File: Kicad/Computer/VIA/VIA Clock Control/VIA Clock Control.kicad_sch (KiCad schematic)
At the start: 14 parts, among them IC10 74LVC1G157GV-Q100H, IC2 AP7365-33WG-7, IC7 74LVC74APW,118, IC8 74LVC257APW,118, IC9 74LVC257APW,118, J1 Conn_02x16_Counter_Clockwise

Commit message: Added a VIA Board.
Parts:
- J1: footprint SamacSys_Parts:DIP-32_Board_W22.86mm -> SamacSys_Parts:DIP-32_Board_W15.24mm
- renumbered R1 to R2
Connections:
- net 5V: now also J1.1 (Pin_1), J1.17 (Pin_17); no longer J1.24 (Pin_24), J1.8 (Pin_8)
- net CH0_{OUT}: now also J1.29 (Pin_29); no longer J1.28 (Pin_28)
- net CH1_{OUT}: now also J1.30 (Pin_30); no longer J1.29 (Pin_29)
- net CH2_{OUT}: now also J1.31 (Pin_31); no longer J1.30 (Pin_30)
- net GND: now also J1.13 (Pin_13), J1.20 (Pin_20), J1.28 (Pin_28), J1.5 (Pin_5); no longer J1.15 (Pin_15), J1.18 (Pin_18), J1.2 (Pin_2), J1.31 (Pin_31)
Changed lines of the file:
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@@
   (junction (at 196.85 59.055) (diameter 0) (color 0 0 0 0)
   )
-  (no_connect (at 4.445 48.26))
+  (no_connect (at 4.445 50.8))
   (no_connect (at 4.445 76.2))
-  (no_connect (at 4.445 78.74))
+  (no_connect (at 4.445 83.82))
   (no_connect (at 4.445 86.36))
   (no_connect (at 17.145 48.26))
   (no_connect (at 17.145 73.66))
   (no_connect (at 4.445 71.12))
-  (no_connect (at 17.145 78.74))
+  (no_connect (at 17.145 68.58))
   (no_connect (at 17.145 63.5))
   (no_connect (at 17.145 81.28))
-  (no_connect (at 17.145 86.36))
+  (no_connect (at 17.145 83.82))
   (no_connect (at 17.145 60.96))
   (no_connect (at 4.445 81.28))
@@
   (no_connect (at 128.27 139.7))
   (no_connect (at 94.615 63.5))
-  (no_connect (at 4.445 58.42))
+  (no_connect (at 4.445 66.04))
   (no_connect (at 4.445 73.66))
   (no_connect (at 222.25 64.135))
@@
     (effects (font (size 1.27 1.27)) (justify right bottom))
   )
-  (label "CH0_{OUT}" (at 17.145 58.42 0) (fields_autoplaced)
+  (label "CH0_{OUT}" (at 17.145 55.88 0) (fields_autoplaced)
     (effects (font (size 1.27 1.27)) (justify left bottom))
   )
@@
     (effects (font (size 1.27 1.27)) (justify left bottom))
   )
+  (label "GND" (at 4.445 78.74 180) (fields_autoplaced)
+    (effects (font (size 1.27 1.27)) (justify right bottom))
+  )
   (label "CLK÷2" (at 56.515 96.52 180) (fields_autoplaced)
     (effects (font (size 1.27 1.27)) (justify right bottom))
@@
     (effects (font (size 1.27 1.27)) (justify right bottom))
   )
-  (label "CH1_{OUT}" (at 17.145 55.88 0) (fields_autoplaced)
-    (effects (font (size 1.27 1.27)) (justify left bottom))
+  (label "CH1_{OUT}" (at 17.145 53.34 0) (fields_autoplaced)
+    (effects (font (size 1.27 1.27)) (justify left bottom))
+  )
+  (label "GND" (at 4.445 58.42 180) (fields_autoplaced)
+    (effects (font (size 1.27 1.27)) (justify right bottom))
   )
   (label "GND" (at 56.515 121.92 180) (fields_autoplaced)
@@
     (effects (font (size 1.27 1.27)) (justify right bottom))
   )
+  (label "GND" (at 17.145 58.42 0) (fields_autoplaced)
+    (effects (font (size 1.27 1.27)) (justify left bottom))
+  )
   (label "GND" (at 104.775 71.755 0) (fields_autoplaced)
     (effects (font (size 1.27 1.27)) (justify left bottom))
@@
     (effects (font (size 1.27 1.27)) (justify right bottom))
   )
-  (label "GND" (at 4.445 83.82 180) (fields_autoplaced)
-    (effects (font (size 1.27 1.27)) (justify right bottom))
+  (label "GND" (at 17.145 78.74 0) (fields_autoplaced)
+    (effects (font (size 1.27 1.27)) (justify left bottom))
   )
   (label "GND" (at 69.215 60.96 180) (fields_autoplaced)
@@
     (effects (font (size 1.27 1.27)) (justify right bottom))
   )
-  (label "5V" (at 4.445 66.04 180) (fields_autoplaced)
+  (label "5V" (at 4.445 48.26 180) (fields_autoplaced)
     (effects (font (size 1.27 1.27)) (justify right bottom))
   )
@@
     (effects (font (size 1.27 1.27)) (justify left bottom))
   )
-  (label "GND" (at 17.145 83.82 0) (fields_autoplaced)
-    (effects (font (size 1.27 1.27)) (justify left bottom))
-  )
-  (label "5V" (at 17.145 68.58 0) (fields_autoplaced)
-    (effects (font (size 1.27 1.27)) (justify left bottom))
-  )
   (label "Select CLK÷2" (at 29.21 124.46 0) (fields_autoplaced)
     (effects (font (size 1.27 1.27)) (justify left bottom))
@@
     (effects (font (size 1.27 1.27)) (justify left bottom))
   )
-  (label "GND" (at 17.145 50.8 0) (fields_autoplaced)
+  (label "5V" (at 17.145 86.36 0) (fields_autoplaced)
     (effects (font (size 1.27 1.27)) (justify left bottom))
   )
@@
     (effects (font (size 1.27 1.27)) (justify right bottom))
   )
-  (label "CH2_{OUT}" (at 17.145 53.34 0) (fields_autoplaced)
+  (label "CH2_{OUT}" (at 17.145 50.8 0) (fields_autoplaced)
     (effects (font (size 1.27 1.27)) (justify left bottom))
   )
@@
     (effects (font (size 1.27 1.27)) (justify right bottom))
   )
-  (label "GND" (at 4.445 50.8 180) (fields_autoplaced)
-    (effects (font (size 1.27 1.27)) (justify right bottom))
-  )
   (label "~{Reset}" (at 69.215 68.58 180) (fields_autoplaced)
     (effects (font (size 1.27 1.27)) (justify right bottom))
@@
   (symbol (lib_id "HCP65:R_0805") (at 26.035 118.11 270) (unit 1)
     (in_bom yes) (on_board yes) (dnp no)
-    (property "Reference" "R1" (at 27.813 120.65 0)
+    (property "Reference" "R2" (at 27.813 120.65 0)
       (effects (font (size 1.27 1.27)))
     )
@@
     (pin "2")
     (instances
-      (project "Via Clock Control"
+      (project "VIA Clock Control"
         (path "/582a2c40-9bf2-463e-b0f7-d7ac5e4fbba5"
           (reference "R2") (unit 1)
@@
         )
       )
-      (project "Via Clock Control"
+      (project "VIA Clock Control"
         (path "/582a2c40-9bf2-463e-b0f7-d7ac5e4fbba5"
           (reference "C1") (unit 1)
@@
         )
       )
-      (project "Via Clock Control"
+      (project "VIA Clock Control"
         (path "/582a2c40-9bf2-463e-b0f7-d7ac5e4fbba5"
           (reference "IC5") (unit 1)
@@
         )
       )
-      (project "Via Clock Control"
+      (project "VIA Clock Control"
         (path "/582a2c40-9bf2-463e-b0f7-d7ac5e4fbba5"
           (reference "C2") (unit 1)
@@
     (pin "N2")
     (instances
-      (project "Via Clock Control"
+      (project "VIA Clock Control"
         (path "/582a2c40-9bf2-463e-b0f7-d7ac5e4fbba5"
           (reference "S1") (unit 1)
@@
         )
       )
-      (project "Via Clock Control"
+      (project "VIA Clock Control"
         (path "/582a2c40-9bf2-463e-b0f7-d7ac5e4fbba5"
           (reference "C4") (unit 1)
@@
         )
       )
-      (project "Via Clock Control"
+      (project "VIA Clock Control"
         (path "/582a2c40-9bf2-463e-b0f7-d7ac5e4fbba5"
           (reference "C6") (unit 1)
@@
     (pin "15")
     (instances
-      (project "Via Clock Control"
+      (project "VIA Clock Control"
         (path "/582a2c40-9bf2-463e-b0f7-d7ac5e4fbba5"
           (reference "IC8") (unit 1)
@@
       (effects (font (size 1.27 1.27)))
     )
-    (property "Footprint" "SamacSys_Parts:DIP-32_Board_W22.86mm" (at 9.525 66.04 0)
+    (property "Footprint" "SamacSys_Parts:DIP-32_Board_W15.24mm" (at 9.525 66.04 0)
       (effects (font (size 1.27 1.27)) hide)
     )
@@
         )
       )
-      (project "Via Clock Control"
+      (project "VIA Clock Control"
         (path "/582a2c40-9bf2-463e-b0f7-d7ac5e4fbba5"
           (reference "J3") (unit 1)
@@
     (pin "15")
     (instances
-      (project "Via Clock Control"
+      (project "VIA Clock Control"
         (path "/582a2c40-9bf2-463e-b0f7-d7ac5e4fbba5"
           (reference "IC9") (unit 1)
@@
     (pin "5")
     (instances
-      (project "Via Clock Control"
+      (project "VIA Clock Control"
         (path "/582a2c40-9bf2-463e-b0f7-d7ac5e4fbba5"
           (reference "IC10") (unit 1)
@@
     (pin "9")
     (instances
-      (project "Via Clock Control"
+      (project "VIA Clock Control"
         (path "/582a2c40-9bf2-463e-b0f7-d7ac5e4fbba5"
           (reference "IC7") (unit 1)
@@
         )
       )
-      (project "Via Clock Control"
+      (project "VIA Clock Control"
         (path "/582a2c40-9bf2-463e-b0f7-d7ac5e4fbba5"
           (reference "C5") (unit 1)
@@
         )
       )
-      (project "Via Clock Control"
+      (project "VIA Clock Control"
         (path "/582a2c40-9bf2-463e-b0f7-d7ac5e4fbba5"
           (reference "C3") (unit 1)

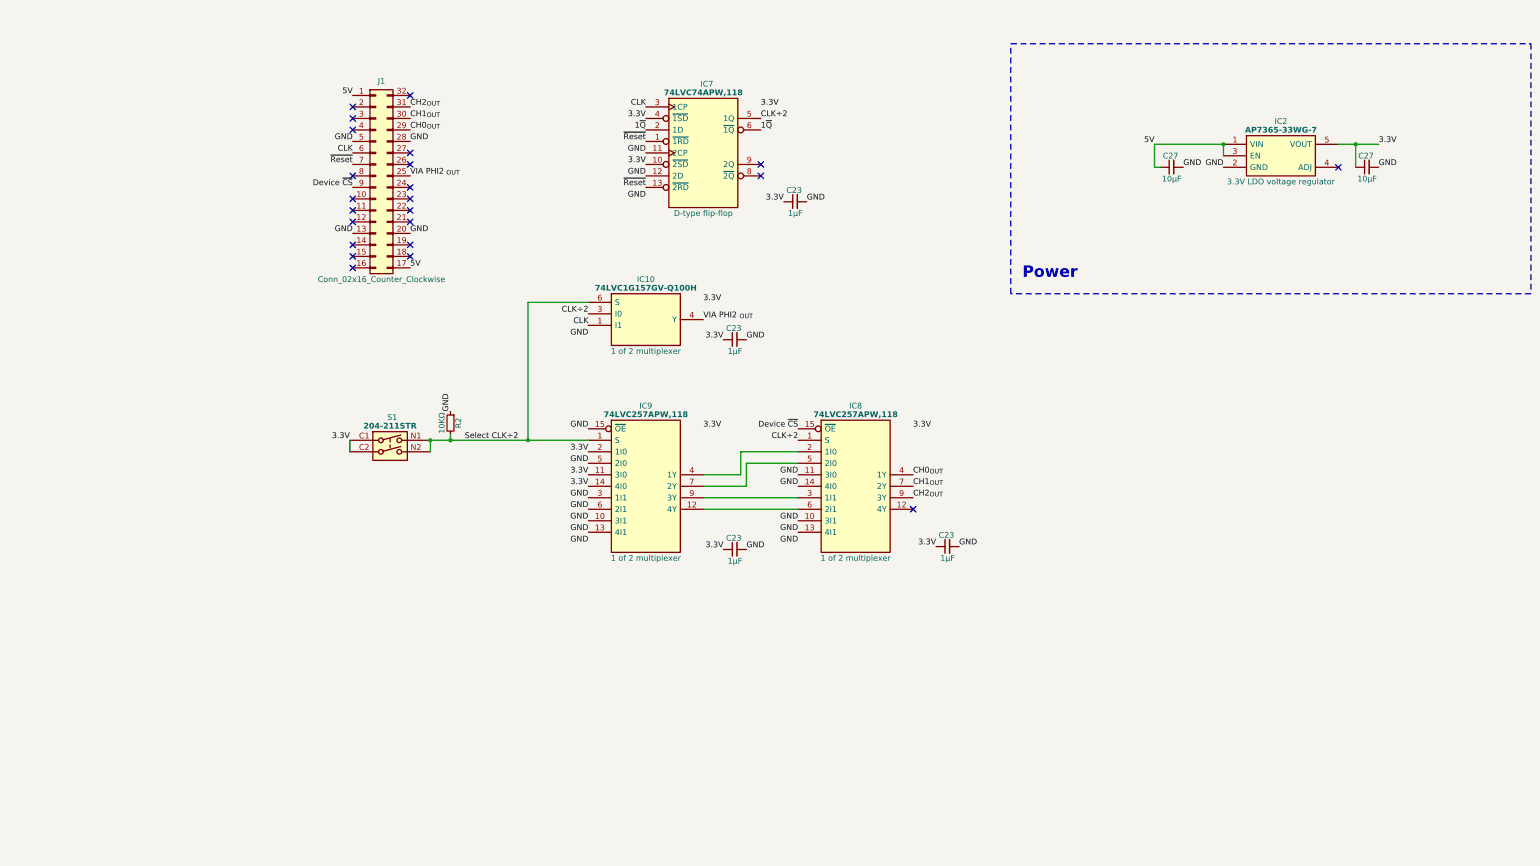
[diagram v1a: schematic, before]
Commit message: Resized VIA and Sound Boards.
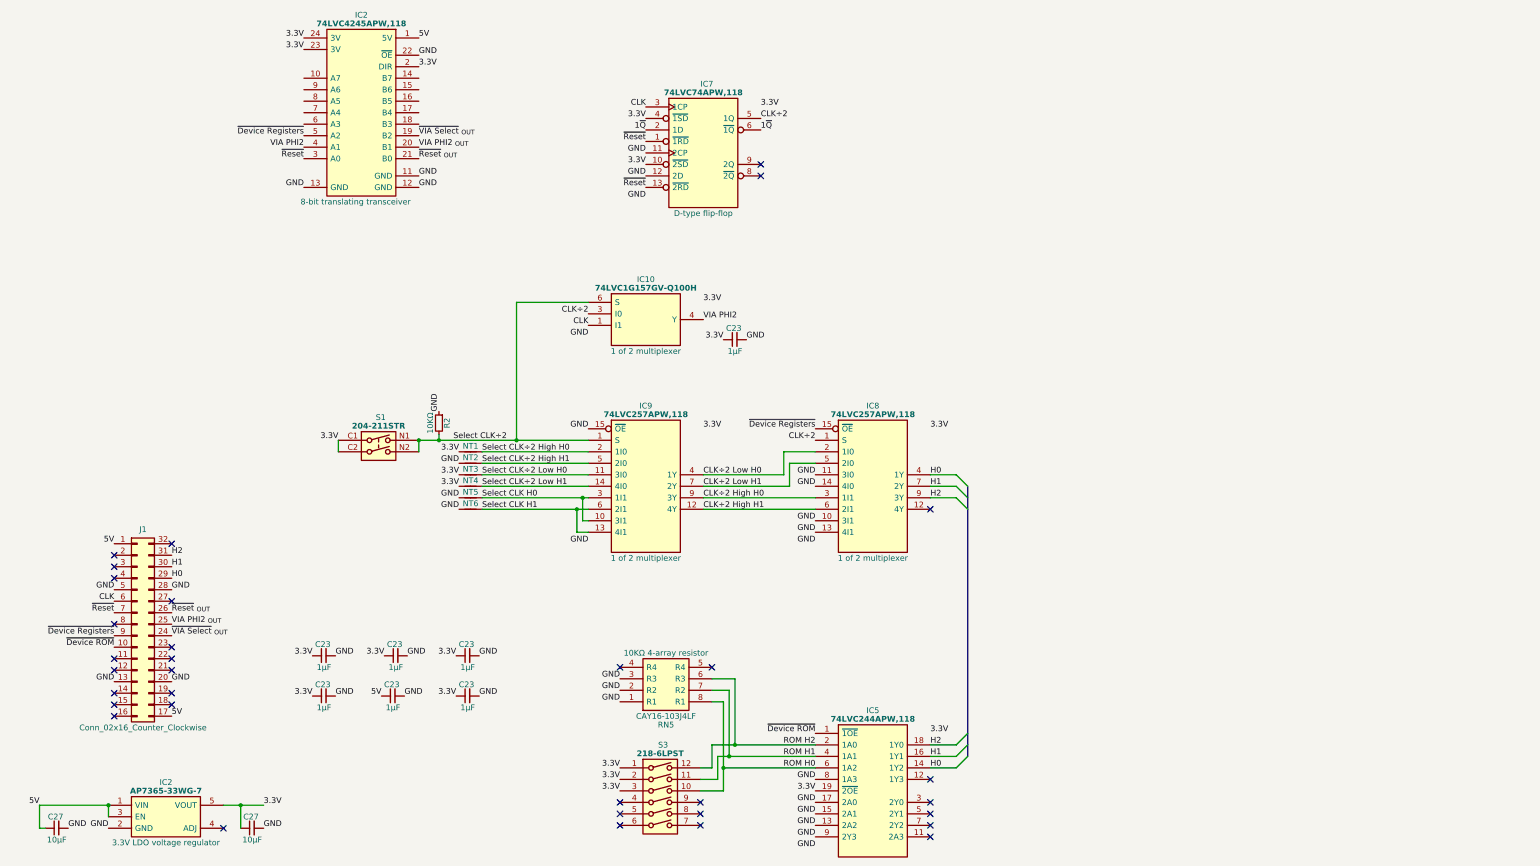
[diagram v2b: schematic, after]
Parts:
- added C23 (x3): 1μF, SamacSys_Parts:C_0805, symbol HCP65:C_0805
- added IC2: 74LVC4245APW,118, SOP65P640X110-24N, symbol Nexperia:74LVC4245APW,118
- added IC5: 74LVC244APW,118, SOP65P640X110-20N, symbol Nexperia:74LVC244APW,118
- added NT1, NT2, NT3, NT4, NT5, NT6: ~, NetTie:NetTie-2_SMD_Pad0.5mm, symbol Device:NetTie_2
- added RN5: CAY16-103J4LF, SamacSys_Parts:CAY16-J4, symbol Bourns:CAY16-103J4LF
- added S3: 218-6LPST, SOIC127P844X265-12N, symbol CTS:218-6LPST
- J1: footprint SamacSys_Parts:DIP-32_Board_W15.24mm -> SamacSys_Parts:DIP-32_Board_W22.86mm
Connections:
- net 3.3V: now also C23.1, C23.1, IC2.2 (DIR), IC2.23 (3V), IC2.24 (3V), IC5.19 (~{2OE}), IC5.20 (3V), NT1.1, NT3.1, NT4.1, S3.1, S3.2, S3.3; no longer IC9.11 (3I0), IC9.14 (4I0), IC9.2 (1I0)
- net 5V: now also C23.1, IC2.1 (5V)
- net GND: now also C23.2, C23.2, C23.2, IC2.11 (GND), IC2.12 (GND), IC2.13 (GND), IC2.22 (~{OE}), IC5.10 (GND), IC5.13 (2A2), IC5.15 (2A1), IC5.17 (2A0), IC5.8 (1A3), IC5.9 (2Y3), NT2.1, NT5.1, NT6.1, RN5.1 (R1), RN5.2 (R2), RN5.3 (R3); no longer IC9.10 (3I1), IC9.13 (4I1), IC9.3 (1I1), IC9.5 (2I0), IC9.6 (2I1)
- net VIA PHI2 _{OUT}: now also IC2.20 (B1); no longer IC10.4 (Y)
- net ~{Reset}: now also IC2.3 (A0)
- net CLK÷2 Low H0: now reaches IC8.2 (1I0), IC9.4 (1Y)
- net CLK÷2 High H0: now reaches IC8.3 (1I1), IC9.9 (3Y)
- net CLK÷2 Low H1: now reaches IC8.5 (2I0), IC9.7 (2Y)
- net CLK÷2 High H1: now reaches IC8.6 (2I1), IC9.12 (4Y)
- net ~{Device ROM}: now reaches J1.10 (Pin_10)
- net ~{Device ROM}: now also IC5.1 (~{1OE})
- net ~{VIA Select} _{OUT}: now reaches J1.24 (Pin_24)
- net ~{VIA Select} _{OUT}: now also IC2.19 (B2)
- net ~{Reset} _{OUT}: now reaches J1.26 (Pin_26)
- net ~{Reset} _{OUT}: now also IC2.21 (B0)
- net CH0_{OUT} renamed H0
- net H0: now also IC5.14 (1Y2)
- net CH1_{OUT} renamed H1
- net H1: now also IC5.16 (1Y1)
- net CH2_{OUT} renamed H2
- net H2: now also IC5.18 (1Y0)
- net Device ~{CS} renamed ~{Device Registers}
- net ~{Device Registers}: now also IC2.5 (A2)
- new net ROM H0: IC5.6 (1A2), RN5.8 (R1), S3.10
- new net ROM H1: IC5.4 (1A1), RN5.7 (R2), S3.11
- new net ROM H2: IC5.2 (1A0), RN5.6 (R3), S3.12
- new net Select CLK H0: IC9.10 (3I1), IC9.3 (1I1), NT5.2
- new net Select CLK H1: IC9.13 (4I1), IC9.6 (2I1), NT6.2
- new net Select CLK÷2 High H0: IC9.2 (1I0), NT1.2
- new net Select CLK÷2 High H1: IC9.5 (2I0), NT2.2
- new net Select CLK÷2 Low H0: IC9.11 (3I0), NT3.2
- new net Select CLK÷2 Low H1: IC9.14 (4I0), NT4.2
- new net VIA PHI2: IC10.4 (Y), IC2.4 (A1)
- no-connect marks 23 -> 33
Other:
- note removed: "Power"
- moved on the sheet: C23, C27, IC2, IC8, J1, R2, S1
